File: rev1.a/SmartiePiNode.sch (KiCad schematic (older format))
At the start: 62 parts, among them CN1 USBMICROb, CN2 SWD, CN3 SX1238_TRX_HEADER, CN4 VIN, SW1 SW_PUSH, U1 ISL91127IR, U2 STM32L052_LQFP48, X1 abm10, X2 ABS25-32.768KHZ-6-T

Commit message: battery sense circuit and new footprint for voltage reg.
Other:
- note added: "battery voltage sensing"
- note removed: "battery voltage sense"
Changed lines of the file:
@@
 $EndComp
 $Comp
-L GND #PWR11
+L GND #PWR01
 U 1 1 5B041A53
 P 3720 7315
-F 0 "#PWR11" H 3720 7065 50  0001 C CNN
+F 0 "#PWR01" H 3720 7065 50  0001 C CNN
 F 1 "GND" H 3725 7142 50  0000 C CNN
 F 2 "" H 3720 7315 50  0001 C CNN
@@
 $EndComp
 $Comp
-L GND #PWR16
+L GND #PWR02
 U 1 1 5B041F18
 P 4975 6485
-F 0 "#PWR16" H 4975 6235 50  0001 C CNN
+F 0 "#PWR02" H 4975 6235 50  0001 C CNN
 F 1 "GND" H 4980 6312 50  0000 C CNN
 F 2 "" H 4975 6485 50  0001 C CNN
@@
 $EndComp
 $Comp
-L GND #PWR17
+L GND #PWR03
 U 1 1 5B04234F
 P 5255 6485
-F 0 "#PWR17" H 5255 6235 50  0001 C CNN
+F 0 "#PWR03" H 5255 6235 50  0001 C CNN
 F 1 "GND" H 5260 6312 50  0000 C CNN
 F 2 "" H 5255 6485 50  0001 C CNN
@@
 $EndComp
 $Comp
-L GND #PWR19
+L GND #PWR04
 U 1 1 5B0423C8
 P 5530 6485
-F 0 "#PWR19" H 5530 6235 50  0001 C CNN
+F 0 "#PWR04" H 5530 6235 50  0001 C CNN
 F 1 "GND" H 5535 6312 50  0000 C CNN
 F 2 "" H 5530 6485 50  0001 C CNN
@@
 $EndComp
 $Comp
-L GND #PWR7
+L GND #PWR05
 U 1 1 5B04306E
 P 2340 6485
-F 0 "#PWR7" H 2340 6235 50  0001 C CNN
+F 0 "#PWR05" H 2340 6235 50  0001 C CNN
 F 1 "GND" H 2345 6312 50  0000 C CNN
 F 2 "" H 2340 6485 50  0001 C CNN
@@
 $EndComp
 $Comp
-L GND #PWR5
+L GND #PWR06
 U 1 1 5B04307C
 P 2060 6485
-F 0 "#PWR5" H 2060 6235 50  0001 C CNN
+F 0 "#PWR06" H 2060 6235 50  0001 C CNN
 F 1 "GND" H 2065 6312 50  0000 C CNN
 F 2 "" H 2060 6485 50  0001 C CNN
@@
 $EndComp
 $Comp
-L GND #PWR4
+L GND #PWR07
 U 1 1 5B04308A
 P 1785 6485
-F 0 "#PWR4" H 1785 6235 50  0001 C CNN
+F 0 "#PWR07" H 1785 6235 50  0001 C CNN
 F 1 "GND" H 1790 6312 50  0000 C CNN
 F 2 "" H 1785 6485 50  0001 C CNN
@@
 $EndComp
 $Comp
-L GND #PWR8
+L GND #PWR08
 U 1 1 5B043F5D
 P 2705 7280
-F 0 "#PWR8" H 2705 7030 50  0001 C CNN
+F 0 "#PWR08" H 2705 7030 50  0001 C CNN
 F 1 "GND" H 2710 7107 50  0000 C CNN
 F 2 "" H 2705 7280 50  0001 C CNN
@@
 $EndComp
 $Comp
-L GND #PWR13
+L GND #PWR09
 U 1 1 5B044D4C
 P 4485 7315
-F 0 "#PWR13" H 4485 7065 50  0001 C CNN
+F 0 "#PWR09" H 4485 7065 50  0001 C CNN
 F 1 "GND" H 4490 7142 50  0000 C CNN
 F 2 "" H 4485 7315 50  0001 C CNN
@@
 $EndComp
 $Comp
-L GND #PWR25
+L GND #PWR010
 U 1 1 5B06F6EF
 P 9930 3790
-F 0 "#PWR25" H 9930 3540 50  0001 C CNN
+F 0 "#PWR010" H 9930 3540 50  0001 C CNN
 F 1 "GND" H 9935 3617 50  0000 C CNN
 F 2 "" H 9930 3790 50  0001 C CNN
@@
 $EndComp
 $Comp
-L GND #PWR23
+L GND #PWR011
 U 1 1 5B0753BB
 P 6760 3380
-F 0 "#PWR23" H 6760 3130 50  0001 C CNN
+F 0 "#PWR011" H 6760 3130 50  0001 C CNN
 F 1 "GND" H 6765 3207 50  0000 C CNN
 F 2 "" H 6760 3380 50  0001 C CNN
@@
 $EndComp
 $Comp
-L GND #PWR3
+L GND #PWR012
 U 1 1 5B081C3A
 P 1715 4725
-F 0 "#PWR3" H 1715 4475 50  0001 C CNN
+F 0 "#PWR012" H 1715 4475 50  0001 C CNN
 F 1 "GND" H 1720 4552 50  0000 C CNN
 F 2 "" H 1715 4725 50  0001 C CNN
@@
 $EndComp
 $Comp
-L GND #PWR21
+L GND #PWR013
 U 1 1 5B082DC4
 P 5880 3240
-F 0 "#PWR21" H 5880 2990 50  0001 C CNN
+F 0 "#PWR013" H 5880 2990 50  0001 C CNN
 F 1 "GND" H 5885 3067 50  0000 C CNN
 F 2 "" H 5880 3240 50  0001 C CNN
@@
 Connection ~ 10575 2935
 $Comp
-L GND #PWR26
+L GND #PWR014
 U 1 1 5B098D9A
 P 11070 2830
-F 0 "#PWR26" H 11070 2580 50  0001 C CNN
+F 0 "#PWR014" H 11070 2580 50  0001 C CNN
 F 1 "GND" H 11075 2657 50  0000 C CNN
 F 2 "" H 11070 2830 50  0001 C CNN
@@
 	2225 1540 2225 1670
 $Comp
-L GND #PWR6
+L GND #PWR015
 U 1 1 5B0A5E1E
 P 2225 1670
-F 0 "#PWR6" H 2225 1420 50  0001 C CNN
+F 0 "#PWR015" H 2225 1420 50  0001 C CNN
 F 1 "GND" H 2230 1497 50  0000 C CNN
 F 2 "" H 2225 1670 50  0001 C CNN
@@
 +3V3
 $Comp
-L GND #PWR9
+L GND #PWR016
 U 1 1 5B0AC996
 P 3070 1200
-F 0 "#PWR9" H 3070 950 50  0001 C CNN
+F 0 "#PWR016" H 3070 950 50  0001 C CNN
 F 1 "GND" H 3075 1027 50  0000 C CNN
 F 2 "" H 3070 1200 50  0001 C CNN
@@
 SPI2_SCK
 $Comp
-L GND #PWR10
+L GND #PWR017
 U 1 1 5B0AE690
 P 3070 1500
-F 0 "#PWR10" H 3070 1250 50  0001 C CNN
+F 0 "#PWR017" H 3070 1250 50  0001 C CNN
 F 1 "GND" H 3075 1327 50  0000 C CNN
 F 2 "" H 3070 1500 50  0001 C CNN
@@
 	4145 2100 4720 2100
 $Comp
-L GND #PWR14
+L GND #PWR018
 U 1 1 5B0AEB87
 P 4720 2100
-F 0 "#PWR14" H 4720 1850 50  0001 C CNN
+F 0 "#PWR018" H 4720 1850 50  0001 C CNN
 F 1 "GND" H 4725 1927 50  0000 C CNN
 F 2 "" H 4720 2100 50  0001 C CNN
@@
 	1625 3160 1695 3160
 $Comp
-L GND #PWR2
+L GND #PWR019
 U 1 1 5B0B10C1
 P 1695 3160
-F 0 "#PWR2" H 1695 2910 50  0001 C CNN
+F 0 "#PWR019" H 1695 2910 50  0001 C CNN
 F 1 "GND" H 1700 2987 50  0000 C CNN
 F 2 "" H 1695 3160 50  0001 C CNN
@@
 +VBAT
 Text Notes 5520 575  0    39   ~ 0
-battery voltage sense
+battery voltage sensing
 $Comp
 L CONN_01X05 CN2
@@
 NRST
 $Comp
-L GND #PWR12
+L GND #PWR020
 U 1 1 5B0B8F14
 P 4200 3080
-F 0 "#PWR12" H 4200 2830 50  0001 C CNN
+F 0 "#PWR020" H 4200 2830 50  0001 C CNN
 F 1 "GND" H 4205 2907 50  0000 C CNN
 F 2 "" H 4200 3080 50  0001 C CNN
@@
 $EndComp
 $Comp
-L GND #PWR24
+L GND #PWR021
 U 1 1 5B0C38AE
 P 8160 5860
-F 0 "#PWR24" H 8160 5610 50  0001 C CNN
+F 0 "#PWR021" H 8160 5610 50  0001 C CNN
 F 1 "GND" H 8165 5687 50  0000 C CNN
 F 2 "" H 8160 5860 50  0001 C CNN
@@
 Connection ~ 6235 2750
 $Comp
-L GND #PWR22
+L GND #PWR022
 U 1 1 5B1AE42D
 P 6235 2785
-F 0 "#PWR22" H 6235 2535 50  0001 C CNN
+F 0 "#PWR022" H 6235 2535 50  0001 C CNN
 F 1 "GND" H 6315 2770 50  0000 C CNN
 F 2 "" H 6235 2785 50  0001 C CNN
@@
 	4855 4565 4855 5170
 $Comp
-L GND #PWR15
+L GND #PWR023
 U 1 1 5B1D46F6
 P 4855 5170
-F 0 "#PWR15" H 4855 4920 50  0001 C CNN
+F 0 "#PWR023" H 4855 4920 50  0001 C CNN
 F 1 "GND" H 4860 4997 50  0000 C CNN
 F 2 "" H 4855 5170 50  0001 C CNN
@@
 	1290 5510 1290 5615
 $Comp
-L GND #PWR1
+L GND #PWR024
 U 1 1 5B2467F2
 P 1290 5615
-F 0 "#PWR1" H 1290 5365 50  0001 C CNN
+F 0 "#PWR024" H 1290 5365 50  0001 C CNN
 F 1 "GND" H 1295 5442 50  0000 C CNN
 F 2 "" H 1290 5615 50  0001 C CNN
@@
 	5270 1400 5270 1525
 $Comp
-L GND #PWR18
+L GND #PWR025
 U 1 1 5B27DE3A
 P 5270 1525
-F 0 "#PWR18" H 5270 1275 50  0001 C CNN
+F 0 "#PWR025" H 5270 1275 50  0001 C CNN
 F 1 "GND" H 5275 1352 50  0000 C CNN
 F 2 "" H 5270 1525 50  0001 C CNN
@@
 	5740 1345 5740 1395
 $Comp
-L GND #PWR20
+L GND #PWR026
 U 1 1 5B2802E4
 P 5740 1395
-F 0 "#PWR20" H 5740 1145 50  0001 C CNN
+F 0 "#PWR026" H 5740 1145 50  0001 C CNN
 F 1 "GND" H 5745 1222 50  0000 C CNN
 F 2 "" H 5740 1395 50  0001 C CNN

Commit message: more pcb layout
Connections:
- net VMEASURE: now also U2.12 (IO-FT-ADC_IN2-PA2)
- net VSENSE: now also U2.11 (IO-FT-ADC_IN1-PA1)
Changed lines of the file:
@@
 U 1 1 5B27CCB4
 P 5270 1300
-F 0 "R20" H 5310 1345 50  0000 L CNN
+F 0 "R20" H 5070 1305 50  0000 L CNN
 F 1 "DNP" V 5270 1220 50  0000 L CNN
 F 2 "Resistors_SMD:R_0603" H 5270 1300 50  0001 C CNN
@@
 Wire Wire Line
 	5435 1705 5845 1705
+Wire Wire Line
+	6890 1190 7375 1190
+Text Label 6890 1190 0    60   ~ 0
+VMEASURE
+Wire Wire Line
+	6890 1090 7375 1090
+Text Label 6890 1090 0    60   ~ 0
+VSENSE
 $EndSCHEMATC

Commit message: optimizing nets
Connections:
- net SPI2_NSS_TRX: now also U2.29 (IO-FT-PA8)
- net TRX_DIO0: now also U2.20 (IO-FT-PB2)
- net TRX_DIO1: now also U2.21 (IO-FT-PB10)
- net TRX_DIO2: now also U2.22 (IO-FT-PB11)
- net TRX_DIO5: now also U2.25 (IO-FT-SPI2_NSS-PB12)
- net TRX_MODE: now also U2.15 (IO-TC-ADC_IN5-PA5)
- net TRX_RESET: now also U2.19 (IO-FT-ADC_IN9-PB1)
- net TRX_RXEN: now also U2.17 (IO-FT-ADC_IN7-PA7)
- net TRX_RXTX: now also U2.18 (IO-FT-ADC_IN8-PB0)
- net TRX_TXEN: now also U2.16 (IO-FT-ADC_IN6-PA6)
- net USB_RENUMn: now also U2.38 (IO-FT-PA15)
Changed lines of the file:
@@
 Text Label 6890 1090 0    60   ~ 0
 VSENSE
+Text Label 6785 2490 0    60   ~ 0
+USB_RENUMn
+Wire Wire Line
+	7375 2490 6785 2490
+Text Label 6785 1790 0    60   ~ 0
+SPI2_NSS_TRX
+Wire Wire Line
+	7375 1790 6785 1790
+Text Label 10310 2190 2    60   ~ 0
+TRX_DIO5
+Wire Wire Line
+	10310 2190 9825 2190
+Text Label 7320 1985 2    60   ~ 0
+TRX_DIO4
+Wire Wire Line
+	10310 2090 9825 2090
+Text Label 7310 1885 2    60   ~ 0
+TRX_DIO3
+Wire Wire Line
+	10310 1990 9825 1990
+Text Label 10310 2090 2    60   ~ 0
+TRX_DIO2
+Wire Wire Line
+	10310 1190 9825 1190
+Text Label 10310 1990 2    60   ~ 0
+TRX_DIO1
+Wire Wire Line
+	10310 1090 9825 1090
+Text Label 10310 1190 2    60   ~ 0
+TRX_DIO0
+Wire Wire Line
+	10310 990  9825 990
+Wire Wire Line
+	6890 1690 7375 1690
+Text Label 10310 1090 2    60   ~ 0
+TRX_RESET
+Wire Wire Line
+	6890 1590 7375 1590
+Text Label 10310 990  2    60   ~ 0
+TRX_RXTX
+Wire Wire Line
+	6890 1490 7375 1490
+Text Label 6890 1690 0    60   ~ 0
+TRX_RXEN
+Text Label 6890 1590 0    60   ~ 0
+TRX_TXEN
+Text Label 6890 1490 0    60   ~ 0
+TRX_MODE
 $EndSCHEMATC

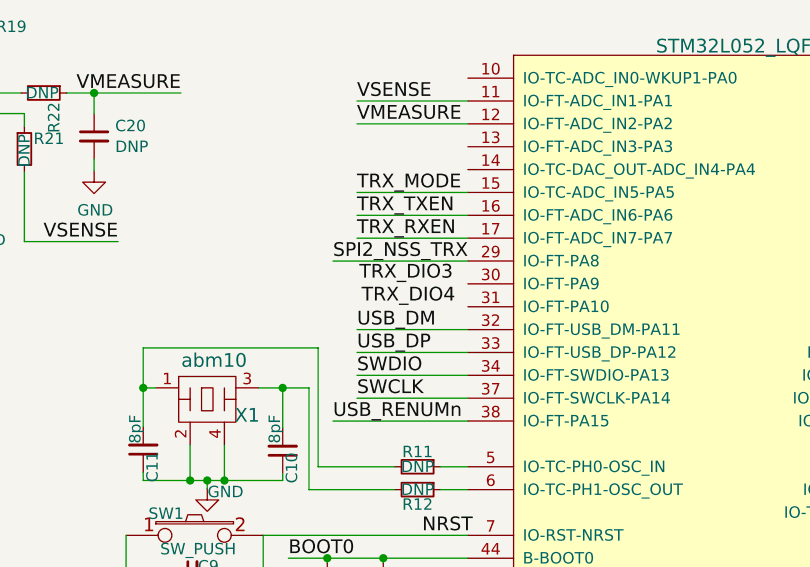
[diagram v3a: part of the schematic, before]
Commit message: finished routing trx
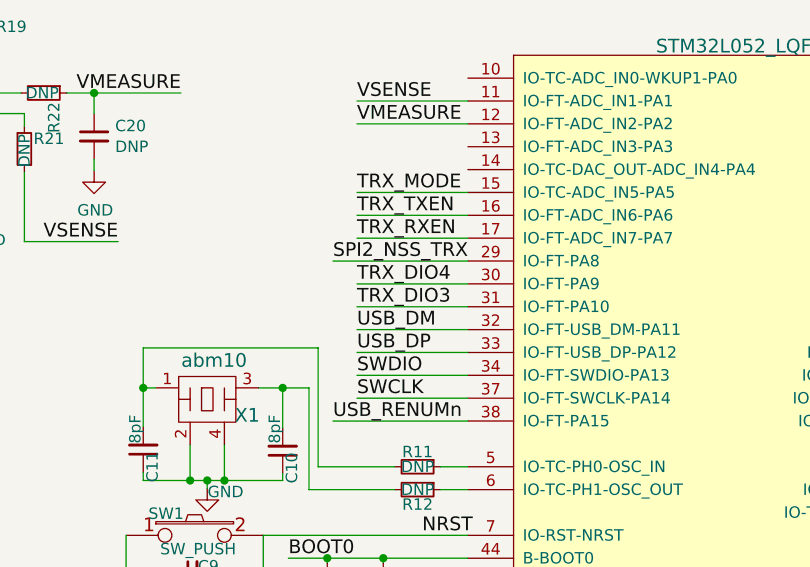
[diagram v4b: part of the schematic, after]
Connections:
- net TRX_DIO3: now also U2.31 (IO-FT-PA10)
- net TRX_DIO4: now also U2.30 (IO-FT-PA9)
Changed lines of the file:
@@
 Wire Wire Line
 	10310 2190 9825 2190
-Text Label 7320 1985 2    60   ~ 0
+Text Label 6890 1890 0    60   ~ 0
 TRX_DIO4
 Wire Wire Line
 	10310 2090 9825 2090
-Text Label 7310 1885 2    60   ~ 0
+Text Label 6890 1990 0    60   ~ 0
 TRX_DIO3
 Wire Wire Line
@@
 Text Label 6890 1490 0    60   ~ 0
 TRX_MODE
+Wire Wire Line
+	6890 1990 7375 1990
+Wire Wire Line
+	6890 1890 7375 1890
 $EndSCHEMATC

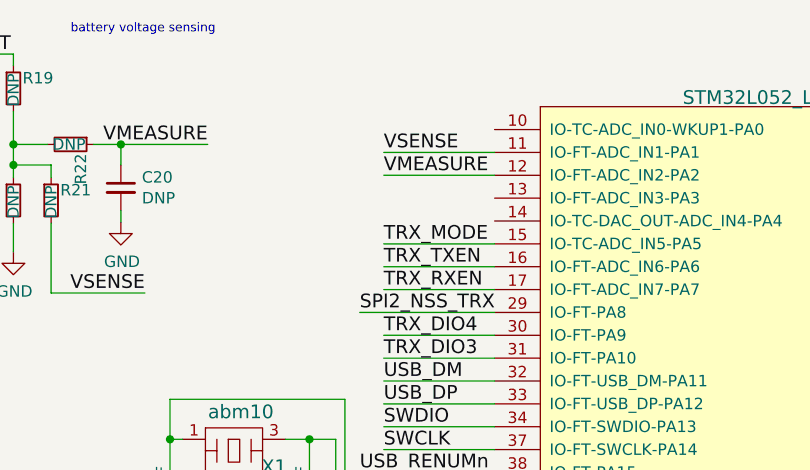
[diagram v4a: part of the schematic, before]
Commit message: everything routed except sensor io header
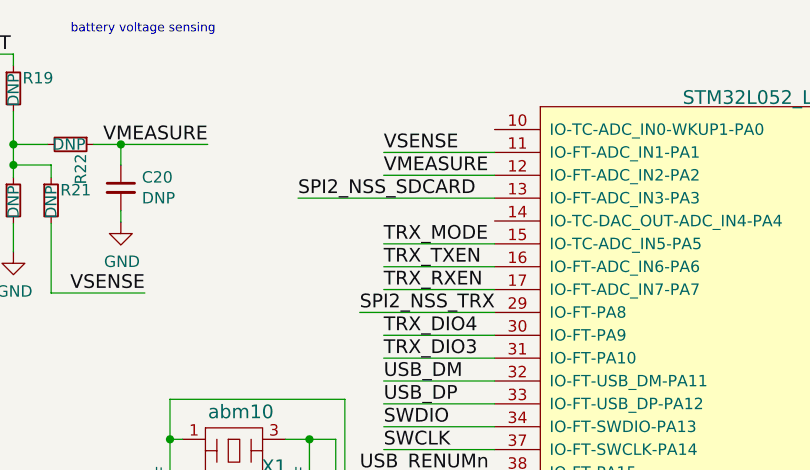
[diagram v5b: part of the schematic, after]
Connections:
- net SPI2_NSS_SDCARD: now also U2.13 (IO-FT-ADC_IN3-PA3)
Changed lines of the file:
@@
 Wire Wire Line
 	6890 1890 7375 1890
+Text Label 6515 1290 0    60   ~ 0
+SPI2_NSS_SDCARD
+Wire Wire Line
+	6515 1290 7375 1290
 $EndSCHEMATC
